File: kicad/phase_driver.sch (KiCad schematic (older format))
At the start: 13 parts, among them Q2 IRF3205, Q5 IRF3205, U3 MIC4605

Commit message: placed and routed; preliminary finished
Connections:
- net HO: now reaches R15.2, U3.3 (HO)
- net LO: now reaches R18.2, U3.8 (LO)
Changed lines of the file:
@@
 $Descr A4 11693 8268
 encoding utf-8
-Sheet 3 4
+Sheet 2 4
 Title ""
 Date ""
@@
 	4600 4550 4550 4550
 Connection ~ 4550 4550
+Text Label 3200 2650 2    50   ~ 0
+HO
+Text Label 3200 3150 2    50   ~ 0
+LO
 $EndSCHEMATC

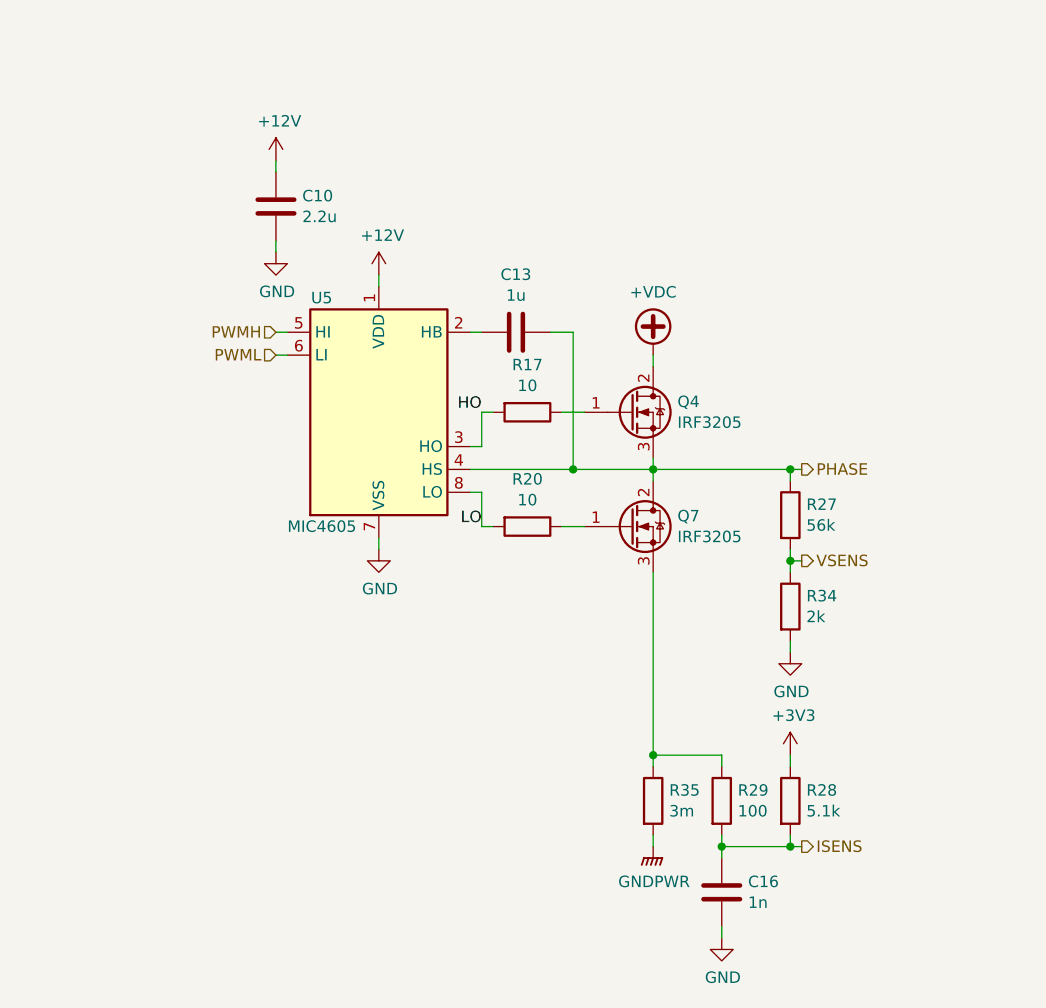
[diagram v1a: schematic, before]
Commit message: made footprint fot mosfets hybrid for TO220 and D2PAK; added jumper instead of 0 Ohm resistor
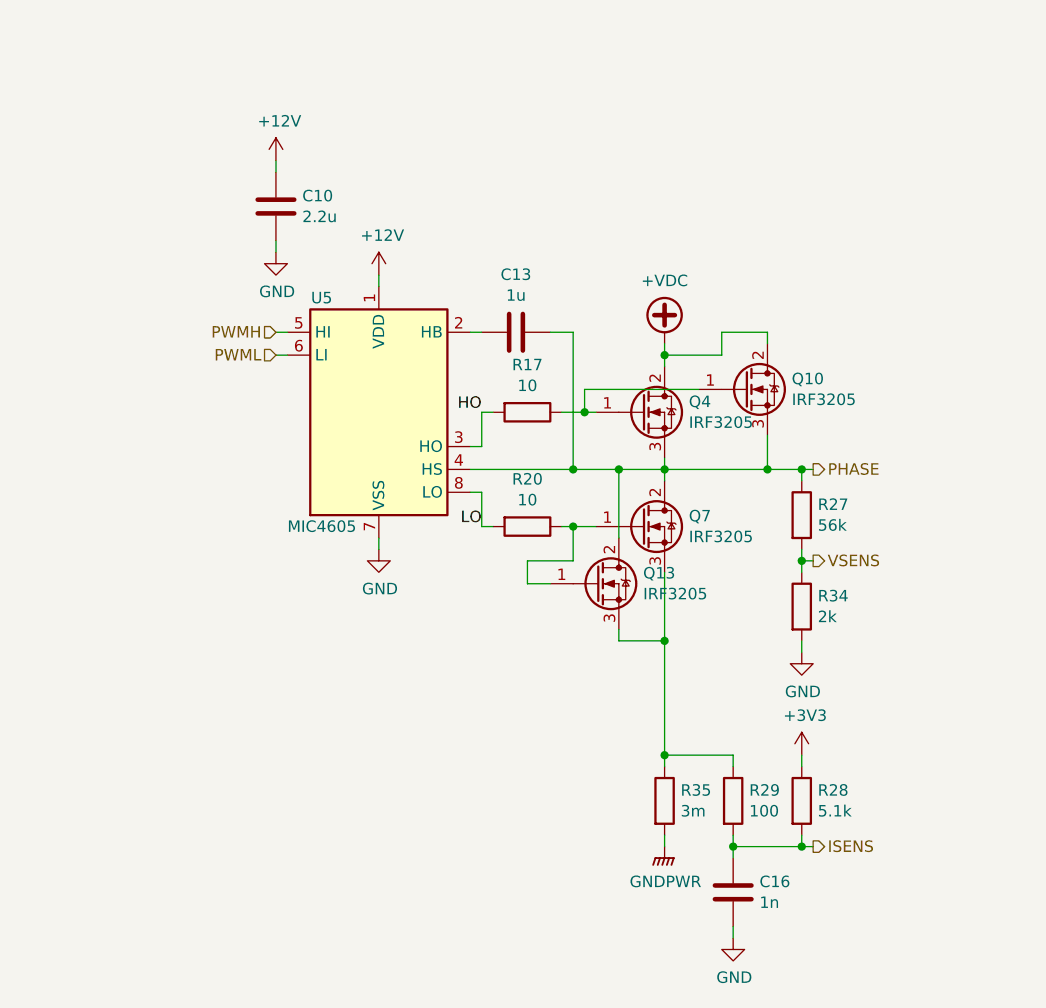
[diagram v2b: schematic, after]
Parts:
- added Q11, Q8: IRF3205, Package_TO_SOT_THT:TO-220-3_Vertical, symbol Transistor_FET:IRF3205
- C11: Voltage Rating DC (none) -> 25
- C14: Voltage Rating DC (none) -> 50
- C8: Voltage Rating DC (none) -> 16
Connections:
- net +VDC: now also Q8.2 (D)
- net PHASE: now also Q11.2 (D), Q8.3 (S)
- net at Q2.1 (G), R15.1: now also Q8.1 (G)
- net at Q5.1 (G), R18.1: now also Q11.1 (G)
- net at Q5.3 (S), R23.1, R31.1: now also Q11.3 (S)
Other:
- moved on the sheet: C16, Q4, Q7, R27, R28, R29, R34, R35

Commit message: added finished adding MPNs to all components
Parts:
- C11: MPN (none) -> 885012106022
- C14: MPN (none) -> 885012206083
- C8: MPN (none) -> GRM188R61E225MA12D; Voltage Rating DC 16 -> 25
- Q11, Q8: value IRF3205 -> IRF100B201; MPN (none) -> IRF100B201
- Q2, Q5: value IRF3205 -> TK160F10N1L; MPN (none) -> TK160F10N1L,LQ
- R15, R18: MPN (none) -> RC0603FR-0710RP
- R21: MPN (none) -> RC0603FR-0756KL
- R22: MPN (none) -> RC0603FR-075K1L
- R23: MPN (none) -> RC0603FR-07100RL
- R30: MPN (none) -> RC0603FR-072KL
- R31: MPN (none) -> WSLF25123L000FEA
- U3: MPN (none) -> MIC4605-1YM-TR
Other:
- moved on the sheet: C10, C13, C16, Q10, Q13, Q4, Q7, R17, R20, R27, R28, R29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

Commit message: finalyzed design
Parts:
- removed U3: MIC4605, Package_SO:SOIC-8_3.9x4.9mm_P1.27mm, symbol Driver_FET:MIC4604YM
- added D3: 1N4148, Diode_SMD:D_SOD-323F, symbol Diode:1N4148
- added U3: IR2102, Package_SO:SOIC-8_3.9x4.9mm_P1.27mm, symbol Driver_FET:IR2102
- C11: value 1u -> 2.2u; MPN 885012106022 -> GRM188R61E225MA12D
- Q2, Q5: Aliexpress (none) -> https://www.aliexpress.com/item//32824255426.html
- R31: Aliexpress (none) -> https://www.aliexpress.com/item//1985453336.html
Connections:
- wire segments 56 -> 62
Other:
- moved on the sheet: C14, C8, Q11, Q2, Q5, Q8, R15, R18, R21, R22, R23, R30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

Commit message: minor cosmetic modifications
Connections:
- wire segments 62 -> 58
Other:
- moved on the sheet: C13, C16, D5, Q10, Q13, Q4, Q7, R17, R20, R27, R28, R29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
